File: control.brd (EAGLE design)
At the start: 100 x 80 mm, 69 parts, among them IC2 XMEGA16A4A, IC3 LM317MBSTT3, IC5 LM358N, Q1 BSS123, Q2 BSS123, Q3 BC548, Q4 BC557C, Q5 TIP41C, Q6 TIP42C, Q7 BC338, Q8 BSS123

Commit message: small improvements
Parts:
- added C11: 100n, resistor:C0805
- added D1: (no value), diode:DO41-7.6
- moved C9 8.47 mm to (40.0, 32.4), turned to 180 degrees
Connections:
- net +12V: now also C11.2, D1.C
- net ADC4: now also D1.A
- net GND: now also C11.1
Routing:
- net +12V: track 90.5 -> 72.6 mm
- net GND: track 2.67 -> 7.54 mm
- net ADC1: track 62.8 -> 58.1 mm, vias 1 -> 0
- net ADC4: track 64.2 -> 68.5 mm
- net EN_A2: track 33.3 -> 35.6 mm

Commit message: duplicated balancer and voltager regulator
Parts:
- added C12: 100n, resistor:C0805K
- added C13: 100p, resistor:C0805K
- added C14: (no value), resistor:E2,5-7
- added C15: 100n, resistor:C0805
- added D2: (no value), diode:DO41-7.6
- added IC1: LM358N, linear:DIL08
- added JP4, JP7: (no value), jumper:JP2
- added JP6: (no value), jumper:JP1
- added JP8: (no value), jumper:JP4
- added Q10: TIP42C, transistor-power:TO220AV
- added Q11: BC338, transistor-npn:TO92-EBC
- added Q12: BC548, transistor-npn:TO92-EBC
- added Q13: BC557C, transistor-pnp:TO92-EBC
- added Q14, Q15, Q16: BSS123, transistor-small-signal:SOT23
- added Q9: TIP41C, transistor-power:TO220AV
- added R10, R11, R14, R15, R17, R57, R58, R59, R60: (no value), resistor:M0805
- added R12, R61: 4R7, resistor-power:KH208R-8
- added R49, R50, R51, R52, R53, R54, R55, R56: (no value), resistor:0207/2V
- added R8, R9: 10R, resistor-power:HPS58
- added U$4, U$5, U$6: STL100NH3LL, teile:PG-TDSON-8
- moved R35 49.0 mm to (24.1, 39.4)
- moved R36 49.0 mm to (24.1, 36.8)
- moved R39 49.0 mm to (24.1, 29.2)
- moved R40 49.0 mm to (24.1, 26.7)
- moved R43 49.0 mm to (29.2, 39.4)
- moved R44 49.0 mm to (29.2, 36.8)
- moved R47 49.0 mm to (29.2, 29.2)
- moved R48 49.0 mm to (29.2, 26.7)
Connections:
- removed net N$10: R44.2
- removed net N$38: R47.2
- removed net N$39: R48.2
- removed net N$5: R43.2
- new net ADC5: JP4.3, JP6.2, R11.2, R47.2, R51.1, R52.1, R8.2
- new net ADC6: IC1.2, JP4.2, R48.2, R55.2, R56.2
- new net ADC7: JP7.2, R43.2, R53.1, R54.1
- new net ADC8: C12.1, C14.+, D2.A, JP7.1, JP8.4, Q9.E, R17.1, R44.2, R49.2, R50.2, R60.2, R61.2
- new net DIS_B: IC2.17, Q14.1
- new net EN_B1: IC2.27, Q15.1
- new net EN_B2: IC2.10, Q16.1
- new net N$12: Q12.C, R8.1
- new net N$2: JP4.1, R10.1, R9.1, U$5.5, U$5.6, U$5.7, U$5.8, U$5.TH
- new net N$3: JP6.1, U$4.5, U$4.6, U$4.7, U$4.8, U$4.TH
- new net N$37: Q13.C, R9.2
- new net N$40: IC1.1, Q12.B, Q13.B
- new net N$41: IC1.3, R10.2, R11.1
- new net N$42: JP8.1, R12.1, U$6.5, U$6.6, U$6.7, U$6.8, U$6.TH
- new net N$43: JP8.3, R12.2
- new net N$45: JP8.2, R61.1
- new net N$46: C13.1, IC1.7, Q11.B
- new net N$47: C13.2, IC1.6, R15.1, R17.2
- new net N$48: IC1.5, IC2.6
- new net N$49: Q10.C, Q9.B, R60.1
- new net N$50: Q11.C, R14.2
- new net N$51: Q10.B, R14.1
- new net N$52: R49.1, R50.1, R51.2, R52.2
- new net N$53: R53.2, R54.2, R55.1, R56.1
- new net N$54: JP7.3, Q12.E, Q13.E
- new net N$55: Q14.3, R59.1, U$6.4
- new net N$56: Q15.3, R58.1, U$4.4
- new net N$57: Q16.3, R57.1, U$5.4
- net +12V: now also C15.2, D2.C, IC1.8, Q10.E, Q9.C, R57.2, R58.2, R59.2
- net GND: now also C12.2, C14.-, C15.1, IC1.4, Q11.E, Q14.2, Q15.2, Q16.2, R15.2, U$4.1, U$4.2, U$4.3, U$5.1, U$5.2, U$5.3, U$6.1, U$6.2, U$6.3
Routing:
- net +12V: track 72.6 -> 143.2 mm
- net ADC8: track 0.00 -> 58.4 mm
- net N$40: track 0.00 -> 32.9 mm
- net ADC7: track 0.00 -> 23.4 mm
- net ADC5: track 0.00 -> 20.9 mm
- net DIS_B: track 0.00 -> 20.4 mm
- net EN_B1: track 0.00 -> 20.1 mm
- net ADC6: track 0.00 -> 18.6 mm
- net N$54: track 0.00 -> 15.3 mm
- net N$2: track 0.00 -> 14.8 mm
- net N$42: track 0.00 -> 14.8 mm
- net N$49: track 0.00 -> 13.7 mm
- net GND: track 7.54 -> 19.9 mm
- net N$41: track 0.00 -> 11.5 mm
- net N$57: track 0.00 -> 8.84 mm, vias 0 -> 1
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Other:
- outline, holes or cut-outs redrawn

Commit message: routing
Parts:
- moved R48 25.9 mm to (24.1, 52.1), turned to 90 degrees
- moved R47 24.1 mm to (21.6, 52.1), turned to 90 degrees
- moved R44 21.8 mm to (11.4, 49.5), turned to 90 degrees
- moved R36 19.3 mm to (6.35, 44.5), flipped to the bottom, turned to 180 degrees
- moved R43 18.3 mm to (14.0, 49.5), turned to 90 degrees
- moved R35 18.2 mm to (7.62, 47.0), flipped to the bottom, turned to 180 degrees
- moved R40 15.2 mm to (24.1, 41.9), turned to 90 degrees
- moved R39 12.8 mm to (22.2, 41.9), turned to 90 degrees
- moved C2 7.65 mm to (8.89, 36.2)
- moved R34 6.63 mm to (6.35, 41.3), flipped to the bottom, turned to 180 degrees
- moved R33 5.39 mm to (6.35, 39.4), flipped to the bottom, turned to 180 degrees
- moved R57 4.02 mm to (39.4, 73.7), flipped to the top
- moved Q16 3.81 mm to (33.0, 76.2)
- moved R37 2.84 mm to (16.5, 45.7), flipped to the bottom
- moved R45 2.54 mm to (17.8, 38.1)
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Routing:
- net +12V: track 143.2 -> 104.9 mm, vias 2 -> 0
- net ADC5: track 20.9 -> 44.0 mm
- net ADC6: track 18.6 -> 38.9 mm
- net N$48: track 0.00 -> 18.0 mm
- net EN_B1: track 20.1 -> 7.44 mm
- net N$57: track 8.84 -> 0.00 mm, vias 1 -> 0
- net ADC8: track 58.4 -> 67.2 mm
- net N$19: track 16.8 -> 20.7 mm
- net N$36: track 7.06 -> 10.2 mm
- net N$23: track 7.99 -> 10.5 mm
- net ADC2: track 47.1 -> 44.5 mm
- net ADC1: track 58.1 -> 55.6 mm
- net GND: track 19.9 -> 17.8 mm
- net N$2: track 14.8 -> 16.8 mm
- net ADC7: track 23.4 -> 21.9 mm
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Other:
- outline, holes or cut-outs redrawn

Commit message: routing, voltage dividers
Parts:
- added X1, X2: (no value), con-wago-508:W237-4P
- moved R37 4.58 mm to (12.7, 48.3)
- moved R57 2.84 mm to (36.8, 74.9)
- moved R35 2.84 mm to (6.35, 44.5)
- moved R43 2.54 mm to (11.4, 49.5)
- moved R44 2.54 mm to (14.0, 49.5)
- moved R36 2.54 mm to (6.35, 47.0)
- moved C4 2.29 mm to (29.8, 47.0)
- moved R38 2.01 mm to (18.4, 47.6)
- moved R40 0.90 mm to (24.8, 42.5)
- moved R39 0.64 mm to (22.2, 42.5)
- moved R41 0.63 mm to (9.53, 31.8)
- moved R42 0.63 mm to (12.1, 31.8)
- moved R34 0.63 mm to (6.35, 41.9)
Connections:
- net ADC7: now also R44.2; no longer R43.2
- net ADC8: now also R43.2; no longer R44.2
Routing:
- net N$21: track 0.00 -> 20.1 mm, vias 0 -> 1
- net N$20: track 0.00 -> 19.3 mm, vias 0 -> 1
- net N$22: track 8.43 -> 13.1 mm
- net N$48: track 18.0 -> 22.3 mm, vias 0 -> 1
- net N$57: track 0.00 -> 3.52 mm, vias 0 -> 1
- net N$24: track 0.00 -> 3.34 mm
- net N$25: track 0.00 -> 3.15 mm
- net +3V3: track 63.8 -> 65.6 mm
- net ADC7: track 21.9 -> 23.5 mm
- net DIS_A: track 37.6 -> 39.1 mm
- net N$23: track 10.5 -> 11.1 mm

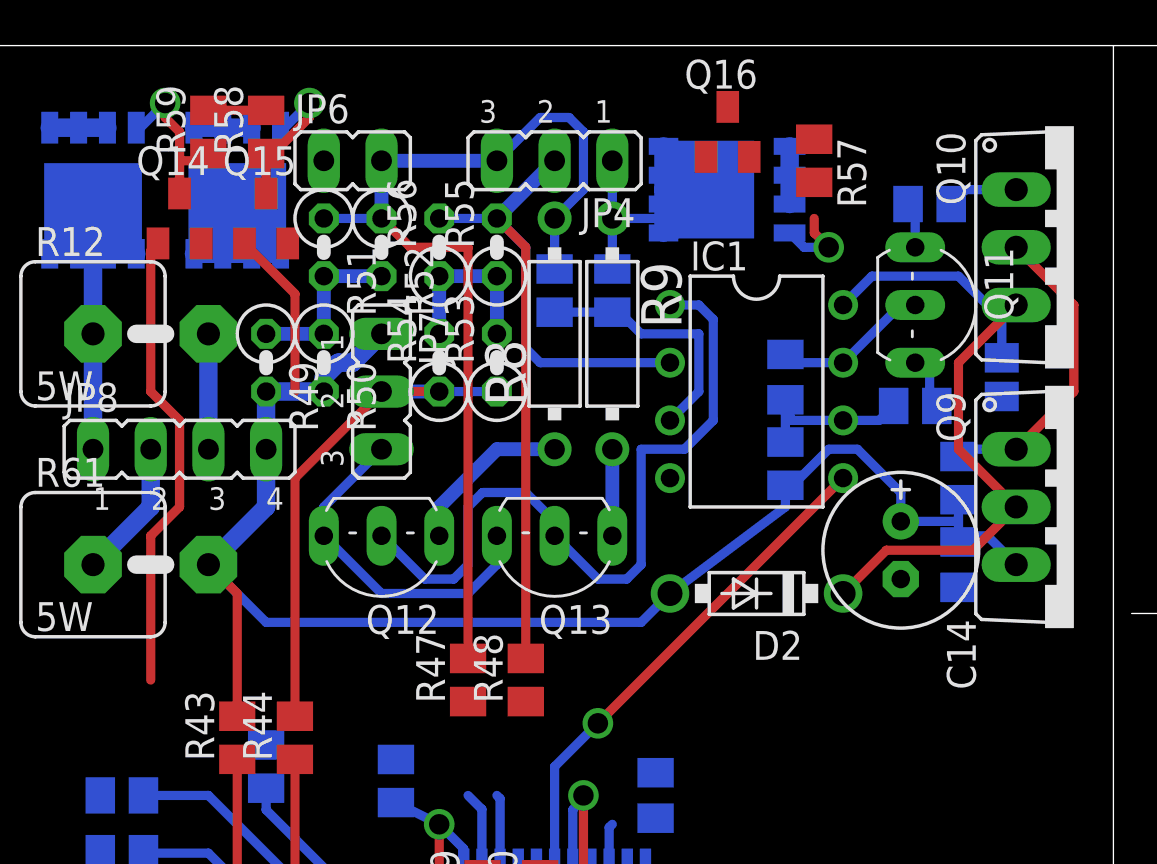
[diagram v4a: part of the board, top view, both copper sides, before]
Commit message: opamp gateswap, fet driver move
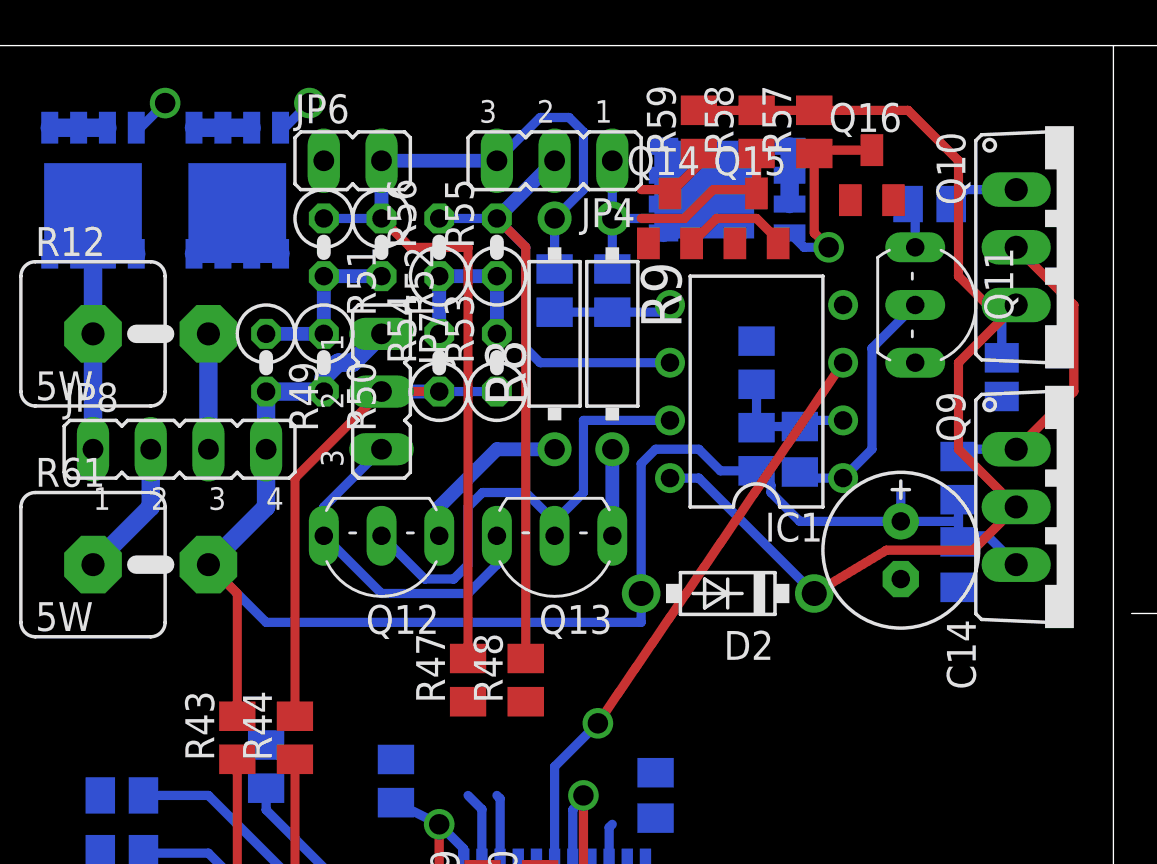
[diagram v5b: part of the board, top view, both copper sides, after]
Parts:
- moved Q14 21.6 mm to (30.5, 72.4)
- moved Q15 21.6 mm to (34.3, 72.4)
- moved R58 21.6 mm to (34.3, 76.2)
- moved R59 21.6 mm to (31.8, 76.2)
- moved R15 7.24 mm to (34.3, 66.0), turned to 90 degrees
- moved Q16 6.63 mm to (39.4, 74.3)
- moved C13 3.24 mm to (36.2, 62.2), turned to 90 degrees
- moved R17 1.42 mm to (34.3, 62.2)
- moved D2 1.27 mm to (33.0, 55.9)
- moved R57 1.27 mm to (36.8, 76.2), turned to 90 degrees
- turned IC1 to 90 degrees
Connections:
- net ADC6: now also IC1.6; no longer IC1.2
- net N$40: now also IC1.7; no longer IC1.1
- net N$41: now also IC1.5; no longer IC1.3
- net N$46: now also IC1.1; no longer IC1.7
- net N$47: now also IC1.2; no longer IC1.6
- net N$48: now also IC1.3; no longer IC1.5
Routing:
- net DIS_B: track 20.4 -> 0.00 mm
- net +12V: track 104.9 -> 123.6 mm
- net N$40: track 32.9 -> 21.4 mm
- net EN_B1: track 7.44 -> 0.00 mm
- net N$41: track 11.5 -> 5.53 mm
- net N$57: track 3.52 -> 8.98 mm
- net ADC8: track 66.9 -> 71.5 mm
- net N$46: track 6.95 -> 11.0 mm
- net N$48: track 22.3 -> 26.3 mm
- net N$56: track 6.68 -> 9.09 mm
- net GND: track 17.8 -> 20.0 mm
- net N$55: track 7.36 -> 5.35 mm
- net N$47: track 7.56 -> 5.85 mm

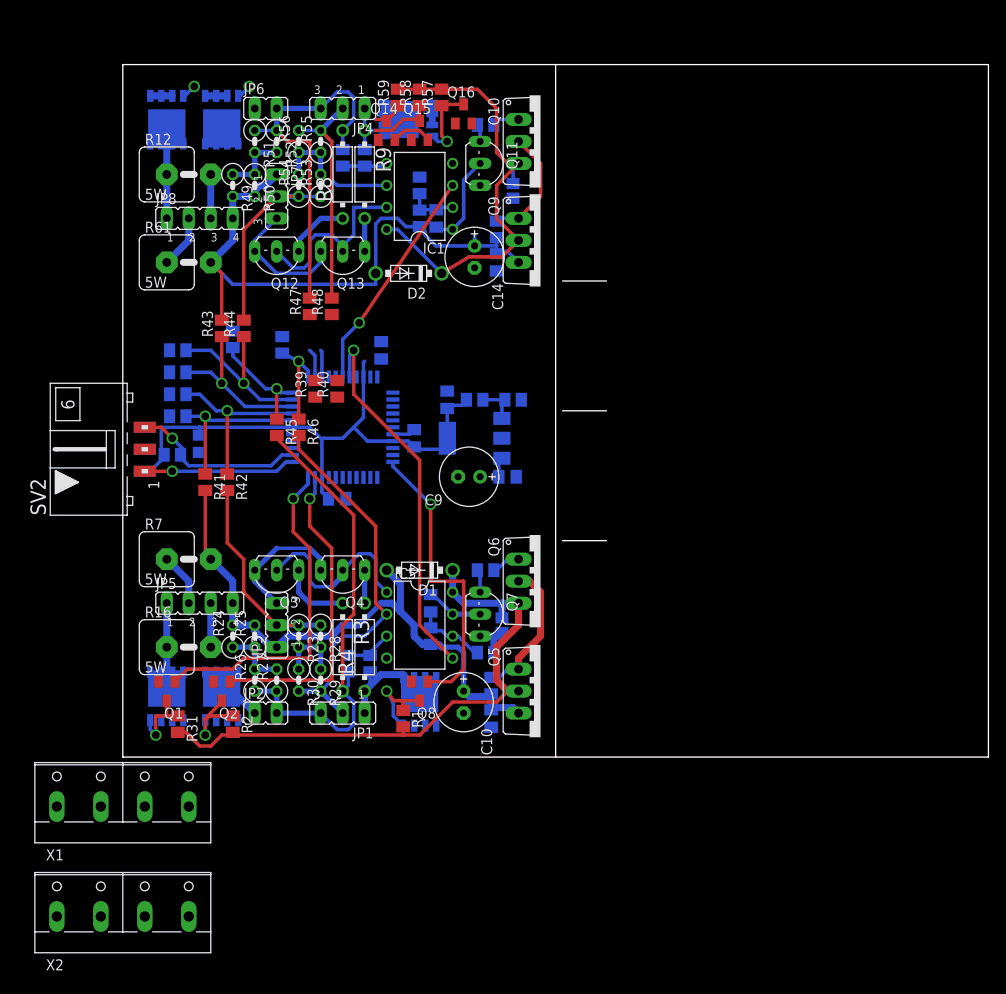
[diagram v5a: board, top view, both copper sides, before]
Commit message: klemmen ersetzt
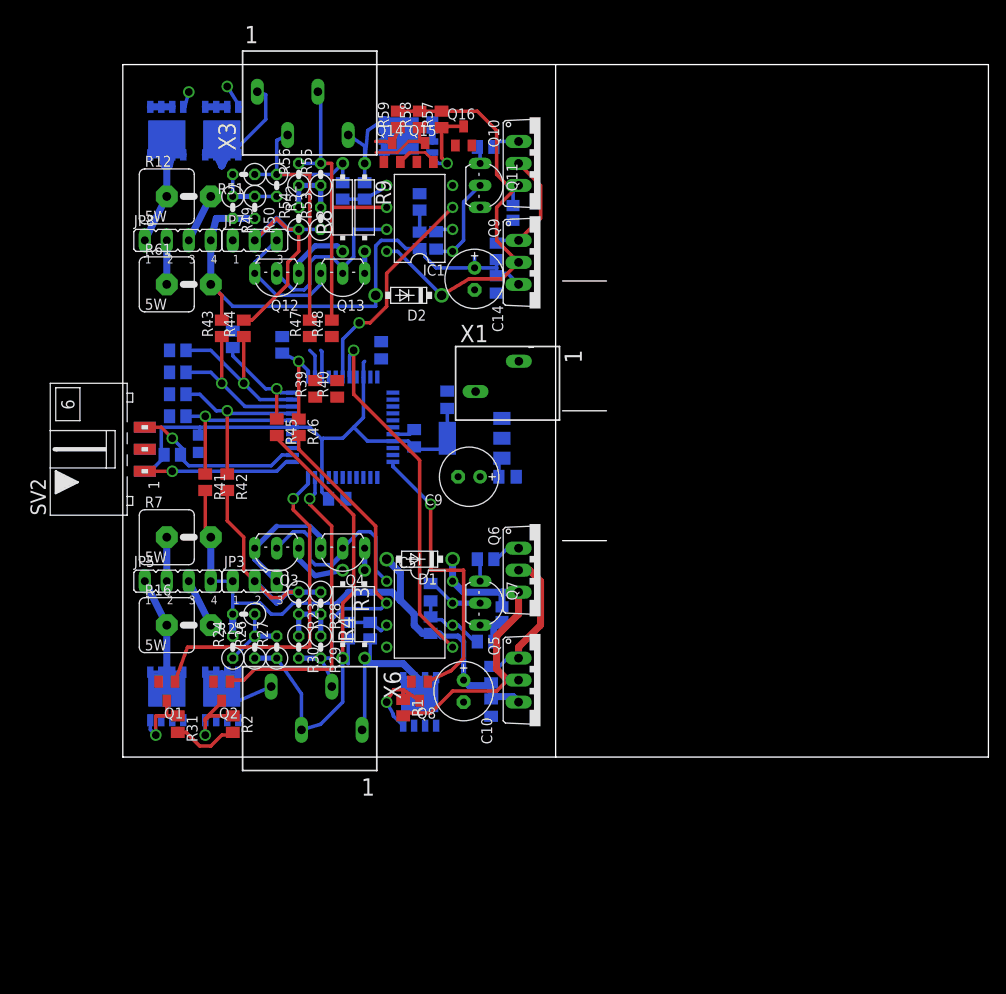
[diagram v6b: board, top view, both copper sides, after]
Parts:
- removed JP1, JP4: (no value), jumper:JP2
- removed JP2, JP6: (no value), jumper:JP1
- removed R19, R20: (no value), resistor:M0805
- removed X2: (no value), con-wago-508:W237-4P
- added X3, X6: 250-204, con-wago_250:P-250-204
- X1: value (none) -> 250-202/000-002; device con-wago-508:W237-4P -> con-wago_250:P-250-202
- moved X1 65.6 mm to (44.5, 43.2)
- moved JP3 5.68 mm to (15.2, 20.3), turned to 0 degrees
- moved JP7 5.68 mm to (15.2, 59.7), turned to 0 degrees
- moved R52 5.08 mm to (17.8, 66.0)
- moved R51 4.02 mm to (14.0, 67.3), turned to 180 degrees
- moved R53 3.81 mm to (22.9, 62.2)
- moved R54 3.81 mm to (20.3, 62.2)
- moved R10 3.81 mm to (27.9, 65.4)
- moved R11 3.81 mm to (25.4, 65.4)
- moved R3 3.81 mm to (25.4, 16.5)
- moved R4 3.81 mm to (27.9, 16.5)
- moved R55 3.81 mm to (22.9, 67.3)
- moved R56 3.81 mm to (20.3, 67.3)
- moved R8 3.81 mm to (25.4, 63.5)
- moved R9 3.81 mm to (27.9, 63.5)
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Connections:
- removed net N$27: IC3.1, R19.2, R20.1
- net +3V3: no longer R20.2
- net ADC1: now also X6.L3; no longer JP1.3, JP2.2
- net ADC2: now also X6.L2; no longer JP1.2
- net ADC5: now also X3.L2; no longer JP4.3, JP6.2
- net ADC6: now also X3.L3; no longer JP4.2
- net GND: now also IC3.1; no longer R19.1
- net N$1: now also X6.L1; no longer JP1.1
- net N$2: now also X3.L4; no longer JP4.1
- net N$3: now also X3.L1; no longer JP6.1
- net N$4: now also X6.L4; no longer JP2.1
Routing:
- net +12V: track 123.6 -> 103.1 mm
- net N$3: track 5.91 -> 19.5 mm
- net ADC7: track 23.5 -> 29.5 mm
- net ADC8: track 71.5 -> 65.9 mm
- net ADC5: track 44.0 -> 38.9 mm
- net N$27: track 4.83 -> 0.00 mm
- net N$1: track 20.3 -> 24.6 mm
- net N$42: track 14.8 -> 18.6 mm
- net N$14: track 14.2 -> 17.3 mm
- net N$4: track 10.9 -> 13.5 mm
- net +3V3: track 65.6 -> 63.3 mm
- net ADC2: track 44.5 -> 42.6 mm
- net N$2: track 16.8 -> 18.6 mm
- net N$56: track 9.09 -> 10.8 mm
- net ADC3: track 25.5 -> 27.1 mm
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
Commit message: routing
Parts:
- C1, C2, C3, C4, C5, C6: value (none) -> 100n
- C10, C14, C9: value (none) -> 100µ
- R1, R15, R18, R2, R21, R31, R33, R34, R35, R36, R37, R38, R39, R40, R57, R58, R59: value (none) -> 10k
- R10, R11, R17, R22, R41, R42, R43, R44, R45, R46, R47, R48, R5, R6: value (none) -> 33k
- R13, R14, R32, R60: value (none) -> 330
- R23, R24, R25, R26, R27, R28, R29, R30, R49, R50, R51, R52, R53, R54, R55, R56: value (none) -> 1
- moved R39 7.01 mm to (21.6, 49.5), flipped to the bottom, turned to 270 degrees
- moved R40 7.01 mm to (24.1, 49.5), flipped to the bottom, turned to 270 degrees
- moved C15 3.86 mm to (45.7, 66.7)
- moved Q10 3.81 mm to (48.3, 72.4)
- moved R60 3.81 mm to (43.2, 62.2)
- moved R14 3.24 mm to (42.5, 73.7), turned to 270 degrees
- moved D2 2.84 mm to (34.3, 55.9), turned to 0 degrees
- moved R59 2.62 mm to (31.1, 76.2)
- moved R57 2.62 mm to (36.2, 76.2)
- moved R58 2.62 mm to (33.7, 76.2)
- moved C14 2.62 mm to (41.3, 52.7)
- moved Q14 2.54 mm to (31.1, 72.4)
- moved Q15 2.54 mm to (34.9, 72.4)
- moved Q16 2.54 mm to (39.4, 74.3)
- moved C12 2.54 mm to (45.7, 54.6), turned to 180 degrees
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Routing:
- net EN_B2: track 0.00 -> 33.3 mm
- net DIS_B: track 0.00 -> 30.3 mm
- net EN_B1: track 0.00 -> 29.3 mm
- net GND: track 20.0 -> 42.9 mm
- net +12V: track 103.1 -> 124.8 mm
- net ADC3: track 27.1 -> 21.0 mm, vias 0 -> 1
- net N$47: track 6.49 -> 12.1 mm
- net N$48: track 25.6 -> 31.1 mm, vias 1 -> 2
- net DIS_A: track 39.5 -> 34.5 mm
- net N$46: track 11.0 -> 15.8 mm
- net EN_A1: track 35.8 -> 31.1 mm
- net ADC1: track 56.4 -> 52.4 mm
- net N$25: track 3.15 -> 7.00 mm, vias 0 -> 1
- net N$24: track 3.34 -> 6.52 mm, vias 0 -> 1
- net N$3: track 19.5 -> 16.6 mm
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
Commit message: GND polygon, schaltplan aufräumen
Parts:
- removed C5: 100n, resistor:C0805K
- added JP1: (no value), jumper:JP2
- moved Q1 2.54 mm to (5.08, 10.2)
- moved U$3 2.54 mm to (5.08, 9.53)
- moved R31 2.54 mm to (6.35, 6.35)
- moved R38 2.01 mm to (19.1, 49.5)
- moved C4 1.42 mm to (29.2, 48.3)
- moved SV2 0.64 mm to (1.91, 35.6)
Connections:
- new net N$27: IC2.13, JP1.1
- new net N$38: IC2.12, JP1.2
- net +12V: now also X1.L2
- net +3V3: no longer C5.1
- net DIS_B: now also IC2.11; no longer IC2.17
- net EN_A2: now also IC2.28; no longer IC2.22
- net EN_B1: now also IC2.14; no longer IC2.27
- net EN_B2: now also IC2.15; no longer IC2.10
- net GND: now also JP1.3, X1.L1; no longer C5.2
- net N$31: now also IC2.6; no longer IC2.7
- net N$48: now also IC2.7; no longer IC2.6
- net N$55: now also U$4.4; no longer U$6.4
- net N$56: now also U$6.4; no longer U$4.4
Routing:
- net +12V: track 124.8 -> 161.2 mm
- net N$56: track 10.8 -> 35.7 mm
- net GND: track 42.9 -> 66.5 mm
- net N$55: track 6.13 -> 24.6 mm
- net ADC7: track 29.5 -> 22.9 mm
- net EN_B2: track 33.3 -> 39.6 mm, vias 0 -> 1
- net ADC8: track 65.4 -> 71.4 mm
- net N$38: track 0.00 -> 5.86 mm
- net EN_B1: track 29.3 -> 35.1 mm, vias 0 -> 1
- net N$27: track 0.00 -> 5.14 mm
- net EN_A2: track 33.3 -> 29.6 mm
- net N$3: track 16.6 -> 13.9 mm
- net N$14: track 17.8 -> 15.2 mm
- net N$23: track 11.1 -> 13.6 mm
- net N$50: track 0.00 -> 2.12 mm
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- added copper zone on layer 1, net GND
- added copper zone on layer 16, net GND
